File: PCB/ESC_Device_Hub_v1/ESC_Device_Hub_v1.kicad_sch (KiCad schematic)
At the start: 130 parts, among them J1 Conn_01x04, J10 Conn_01x06, J11 Conn_01x02, J12 Conn_01x02, J13 Conn_01x02, J14 Conn_01x02, J15 Conn_01x02, J16 Conn_01x02, J17 Conn_01x02, J18 Conn_01x02, J2 Conn_01x04, J20 Conn_01x01, J21 Conn_01x01, J22 Conn_01x02, J23 Conn_01x04, J3 Conn_01x04, J4 Conn_01x04, J5 Conn_01x04, J6 Conn_01x04, J7 Conn_01x06, J8 Conn_01x06, J9 Conn_01x06, SW1 SW_Push, SW2 SW_Push, SW4 SW_DIP_x02, U1 ISO1042BQDWVQ1, U10 LM66100DCK, U11 LM66100DCK, U18 USB_Type-C, U2 MCP2562FD-H/MF, U3 IS25LP064D-JLLE, U4 STM32H563RGVx, U6 TLP293, U7 NJM2884U1-33, U8 RFM-0505S, Y1 FC2012SN 32.768K-70NNA0KC0, Y2 XRCGB25M000FFS1AR0

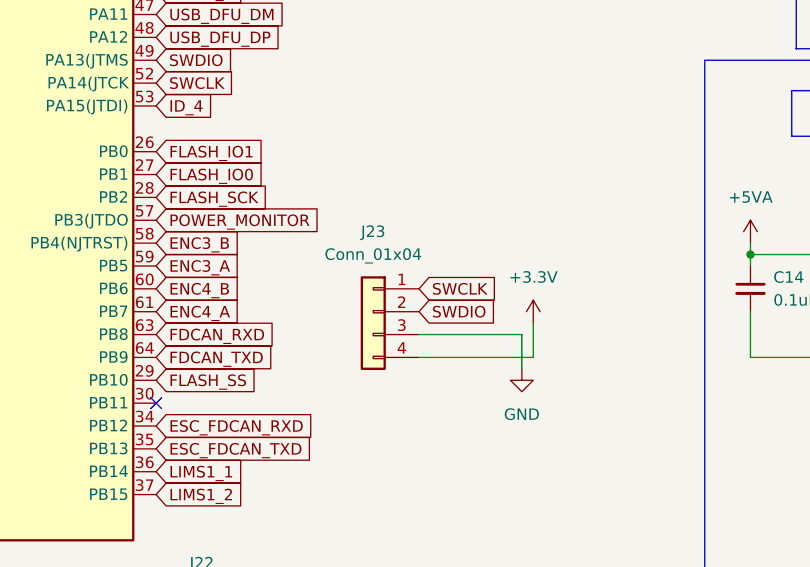
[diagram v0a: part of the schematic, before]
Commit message: PIの追加　基板PCB変更
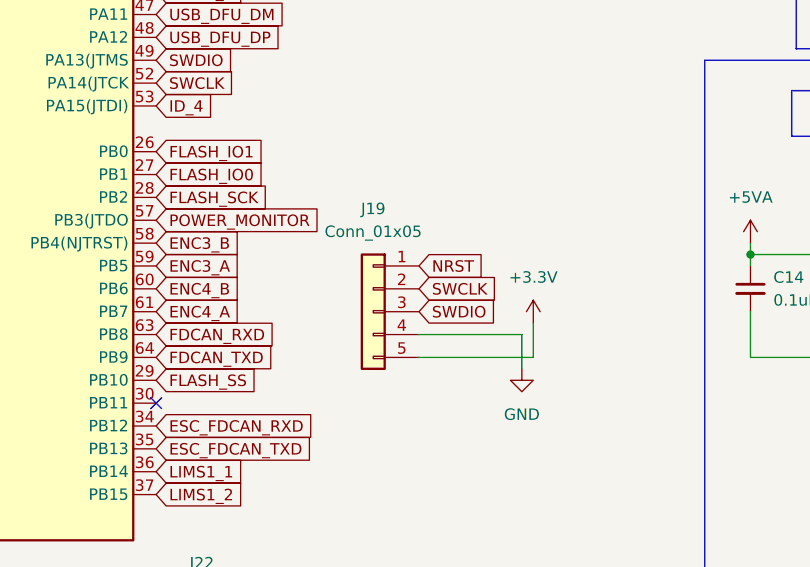
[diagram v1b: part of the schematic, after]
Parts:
- removed J23: Conn_01x04, Connector_PinSocket_2.54mm:PinSocket_1x04_P2.54mm_Vertical, symbol Connector_Generic:Conn_01x04
- added J19: Conn_01x05, Connector_PinSocket_2.54mm:PinSocket_1x05_P2.54mm_Vertical, symbol Connector_Generic:Conn_01x05
- C7: footprint Capacitor_SMD:C_0402_1005Metric_Pad0.74x0.62mm_HandSolder -> Capacitor_SMD:C_0603_1608Metric_Pad1.08x0.95mm_HandSolder
- R3: footprint Resistor_SMD:R_0402_1005Metric_Pad0.72x0.64mm_HandSolder -> Resistor_SMD:R_0603_1608Metric_Pad0.98x0.95mm_HandSolder
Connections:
- net +3.3V: now also J19.5 (Pin_5)
- net GND: now also J19.4 (Pin_4)
- net NRST: now also J19.1 (Pin_1)
- net SWCLK: now also J19.2 (Pin_2)
- net SWDIO: now also J19.3 (Pin_3)
